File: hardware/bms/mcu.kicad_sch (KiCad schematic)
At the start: 0 parts

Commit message: More charger sch progress
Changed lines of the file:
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@@
     (effects (font (size 1.27 1.27)) (justify right))
+  )
+  (hierarchical_label "PWM_OUT1" (shape output) (at 130.81 40.64 0) (fields_autoplaced)
+    (effects (font (size 1.27 1.27)) (justify left))
   )
   (hierarchical_label "MCU_VIN" (shape input) (at 49.53 40.64 180) (fields_autoplaced)
@@
     (effects (font (size 1.27 1.27)) (justify right))
   )
+  (hierarchical_label "PWM_OUT2" (shape output) (at 130.81 44.45 0) (fields_autoplaced)
+    (effects (font (size 1.27 1.27)) (justify left))
+  )
 )

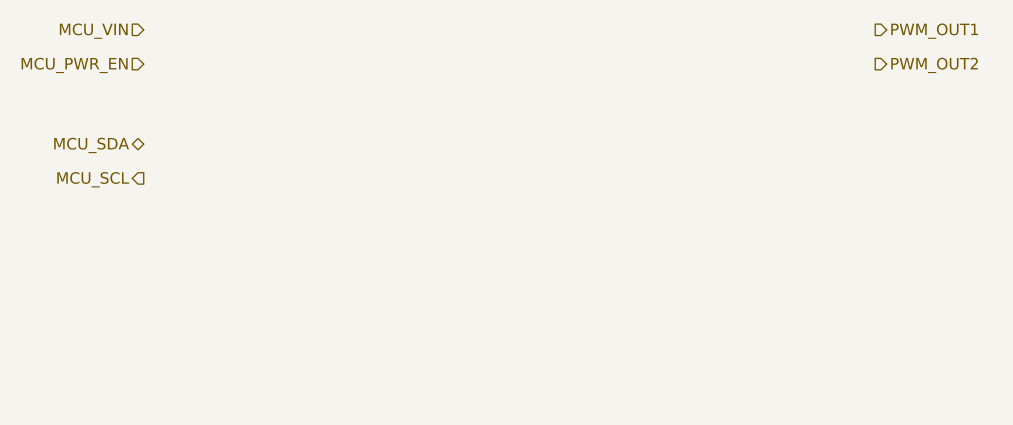
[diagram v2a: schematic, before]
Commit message: Made more progress on charger sch. Need to complete power stage next. Also added diode OR for MCU power conv input. Still deciding on converter selection
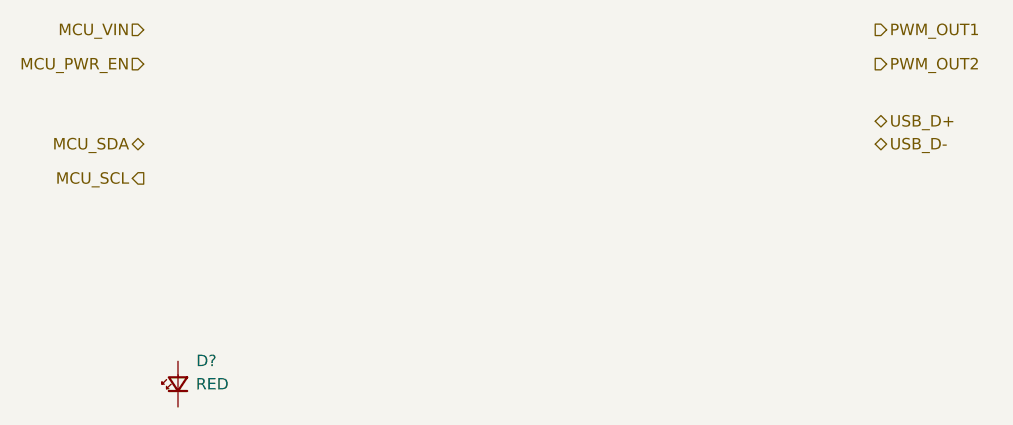
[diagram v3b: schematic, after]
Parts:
- added D?: RED, LED_SMD:LED_0603_1608Metric, symbol Device:LED_Small
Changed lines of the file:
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@@
     (effects (font (size 1.27 1.27)) (justify right))
+  )
+  (hierarchical_label "USB_D+" (shape bidirectional) (at 130.81 50.8 0) (fields_autoplaced)
+    (effects (font (size 1.27 1.27)) (justify left))
   )
   (hierarchical_label "PWM_OUT1" (shape output) (at 130.81 40.64 0) (fields_autoplaced)
@@
     (effects (font (size 1.27 1.27)) (justify right))
   )
+  (hierarchical_label "USB_D-" (shape bidirectional) (at 130.81 53.34 0) (fields_autoplaced)
+    (effects (font (size 1.27 1.27)) (justify left))
+  )
   (hierarchical_label "MCU_SDA" (shape bidirectional) (at 49.53 53.34 180) (fields_autoplaced)
     (effects (font (size 1.27 1.27)) (justify right))
@@
     (effects (font (size 1.27 1.27)) (justify left))
   )
+  (symbol (lib_id "Device:LED_Small") (at 53.34 80.01 90) (unit 1)
+    (in_bom yes) (on_board yes) (dnp no)
+    (property "Reference" "D?" (at 56.5003 77.4194 90)
+      (effects (font (size 1.27 1.27)))
+    )
+    (property "Value" "RED" (at 57.15 80.01 90)
+      (effects (font (size 1.27 1.27)))
+    )
+    (property "Footprint" "LED_SMD:LED_0603_1608Metric" (at 53.34 80.01 90)
+      (effects (font (size 1.27 1.27)) hide)
+    )
+    (property "Datasheet" "~" (at 53.34 80.01 90)
+      (effects (font (size 1.27 1.27)) hide)
+    )
+    (property "MFG" "Würth Elektronik" (at 53.34 80.01 90)
+      (effects (font (size 1.27 1.27)) hide)
+    )
+    (property "MFG PN" "150060RS75000" (at 53.34 80.01 90)
+      (effects (font (size 1.27 1.27)) hide)
+    )
+    (property "VF" "2V" (at 53.34 80.01 90)
+      (effects (font (size 1.27 1.27)) hide)
+    )
+    (pin "1")
+    (pin "2")
+    (instances
+      (project "bms"
+        (path "/a4805e9d-b940-444e-a7cb-db4f4c53ed46/00000000-0000-0000-0000-00006523ab32"
+          (reference "D?") (unit 1)
+        )
+        (path "/a4805e9d-b940-444e-a7cb-db4f4c53ed46/00000000-0000-0000-0000-00006658c265"
+          (reference "D?") (unit 1)
+        )
+      )
+    )
+  )
 )

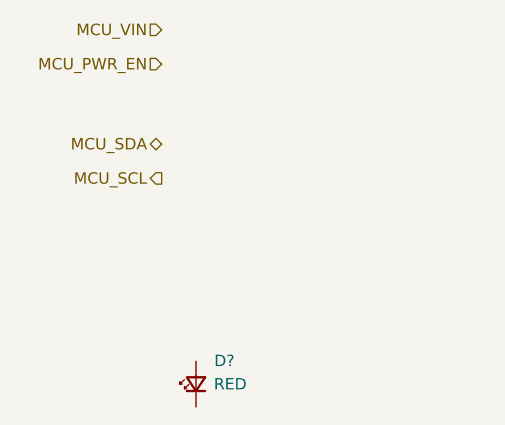
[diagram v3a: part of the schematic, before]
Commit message: Charger schematic complete! Only MCU left.
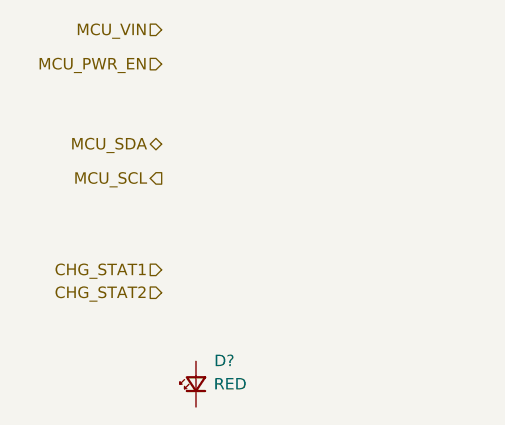
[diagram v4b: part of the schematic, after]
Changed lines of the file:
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@@
     (effects (font (size 1.27 1.27)) (justify left))
+  )
+  (hierarchical_label "CHG_STAT2" (shape input) (at 49.53 69.85 180) (fields_autoplaced)
+    (effects (font (size 1.27 1.27)) (justify right))
   )
   (hierarchical_label "PWM_OUT1" (shape output) (at 130.81 40.64 0) (fields_autoplaced)
@@
     (effects (font (size 1.27 1.27)) (justify left))
   )
+  (hierarchical_label "CHG_STAT1" (shape input) (at 49.53 67.31 180) (fields_autoplaced)
+    (effects (font (size 1.27 1.27)) (justify right))
+  )
   (symbol (lib_id "Device:LED_Small") (at 53.34 80.01 90) (unit 1)

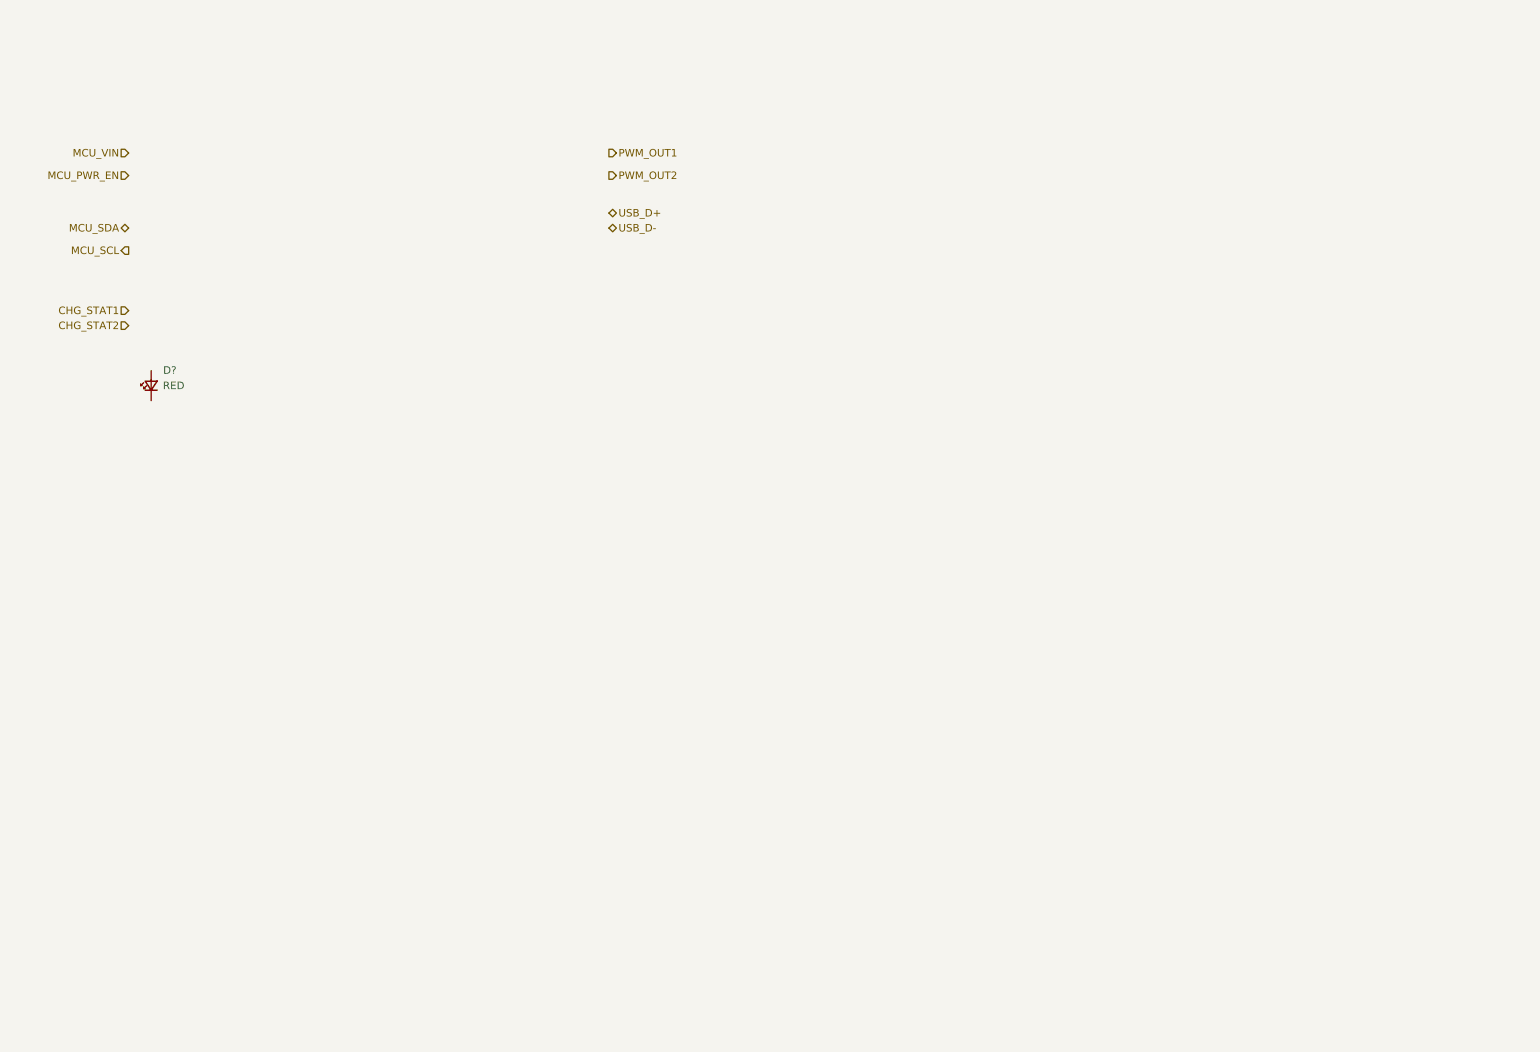
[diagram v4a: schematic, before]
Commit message: Choose MCU as ESP32-C3-MINI. Small form factor with just enough I/O.
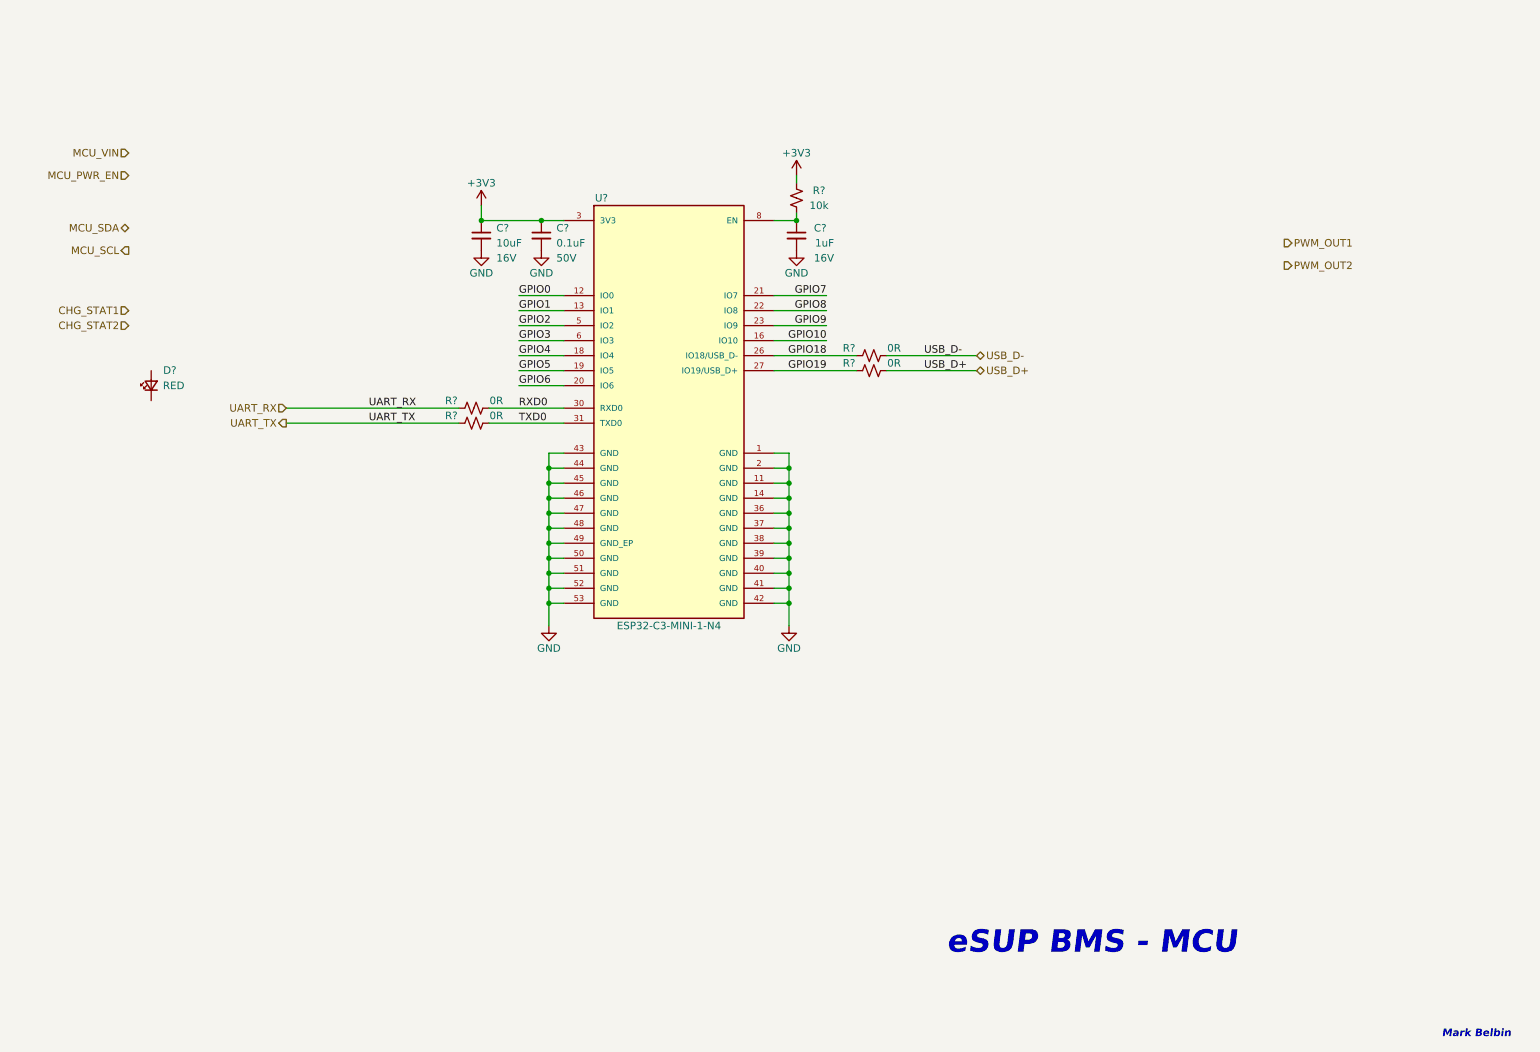
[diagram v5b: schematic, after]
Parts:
- added C?: 0.1uF, Capacitor_SMD:C_0603_1608Metric, symbol Device:C_Small
- added C?: 1uF, Capacitor_SMD:C_0603_1608Metric, symbol Device:C_Small
- added C?: 10uF, Capacitor_SMD:C_0603_1608Metric, symbol Device:C_Small
- added R? (x4): 0R, Resistor_SMD:R_0603_1608Metric, symbol Device:R_Small_US
- added R?: 10k, Resistor_SMD:R_0603_1608Metric, symbol Device:R_Small_US
- added U?: ESP32-C3-MINI-1-N4, bms:ESP32-C3-MINI-1, symbol bms:ESP32-C3-MINI-1-N4
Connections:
- net USB_D+: now also R?.2
- net USB_D-: now also R?.2
- new net: C?.1, R?.2, U?.8 (EN)
- new net: U?.10 (NC), U?.15 (NC), U?.17 (NC), U?.24 (NC), U?.25 (NC), U?.28 (NC), U?.29 (NC), U?.32 (NC), U?.33 (NC), U?.34 (NC), U?.35 (NC), U?.4 (NC), U?.7 (NC), U?.9 (NC)
- new net +3V3: C?.1, C?.1, R?.1, U?.3 (3V3)
- new net GND: C?.2, C?.2, C?.2, U?.1 (GND), U?.11 (GND), U?.14 (GND), U?.2 (GND), U?.36 (GND), U?.37 (GND), U?.38 (GND), U?.39 (GND), U?.40 (GND), U?.41 (GND), U?.42 (GND), U?.43 (GND), U?.44 (GND), U?.45 (GND), U?.46 (GND), U?.47 (GND), U?.48 (GND), U?.49 (GND_EP), U?.50 (GND), U?.51 (GND), U?.52 (GND), U?.53 (GND)
- new net GPIO0: U?.12 (IO0)
- new net GPIO1: U?.13 (IO1)
- new net GPIO10: U?.16 (IO10)
- new net GPIO18: R?.1, U?.26 (IO18/USB_D-)
- new net GPIO19: R?.1, U?.27 (IO19/USB_D+)
- new net GPIO2: U?.5 (IO2)
- new net GPIO3: U?.6 (IO3)
- new net GPIO4: U?.18 (IO4)
- new net GPIO5: U?.19 (IO5)
- new net GPIO6: U?.20 (IO6)
- new net GPIO7: U?.21 (IO7)
- new net GPIO8: U?.22 (IO8)
- new net GPIO9: U?.23 (IO9)
- new net RXD0: R?.2, U?.30 (RXD0)
- new net TXD0: R?.2, U?.31 (TXD0)
- new net UART_RX: R?.1
- new net UART_TX: R?.1
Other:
- note added: "Mark Belbin"
- note added: "eSUP BMS - MCU"

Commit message: Added BJT to enable BMS/MCU when charger input voltage present
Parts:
- added C?: 0.1uF, Capacitor_SMD:C_0603_1608Metric, symbol Device:C_Small
- added D?: WS2812B, LED_SMD:LED_WS2812B_PLCC4_5.0x5.0mm_P3.2mm, symbol LED:WS2812B
- added U?: SN74LXC1T14DCKR, bms:DCK0005A-IPC_C, symbol bms:SN74LXC1T14DCKR
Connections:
- net +3V3: now also U?.1 (VCCI)
- net GND: now also C?.2, D?.3 (VSS), U?.3 (GND)
- new net +5V: C?.1, D?.1 (VDD), U?.5 (VCCO)
- new net RGB_DIN: D?.4 (DIN), U?.4 (Y)
- new net RGB_DIN_ESP: U?.2 (A)
- new net RGB_DOUT: D?.2 (DOUT)
- no-connect marks 0 -> 1
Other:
- moved on the sheet: C?, R?, U?

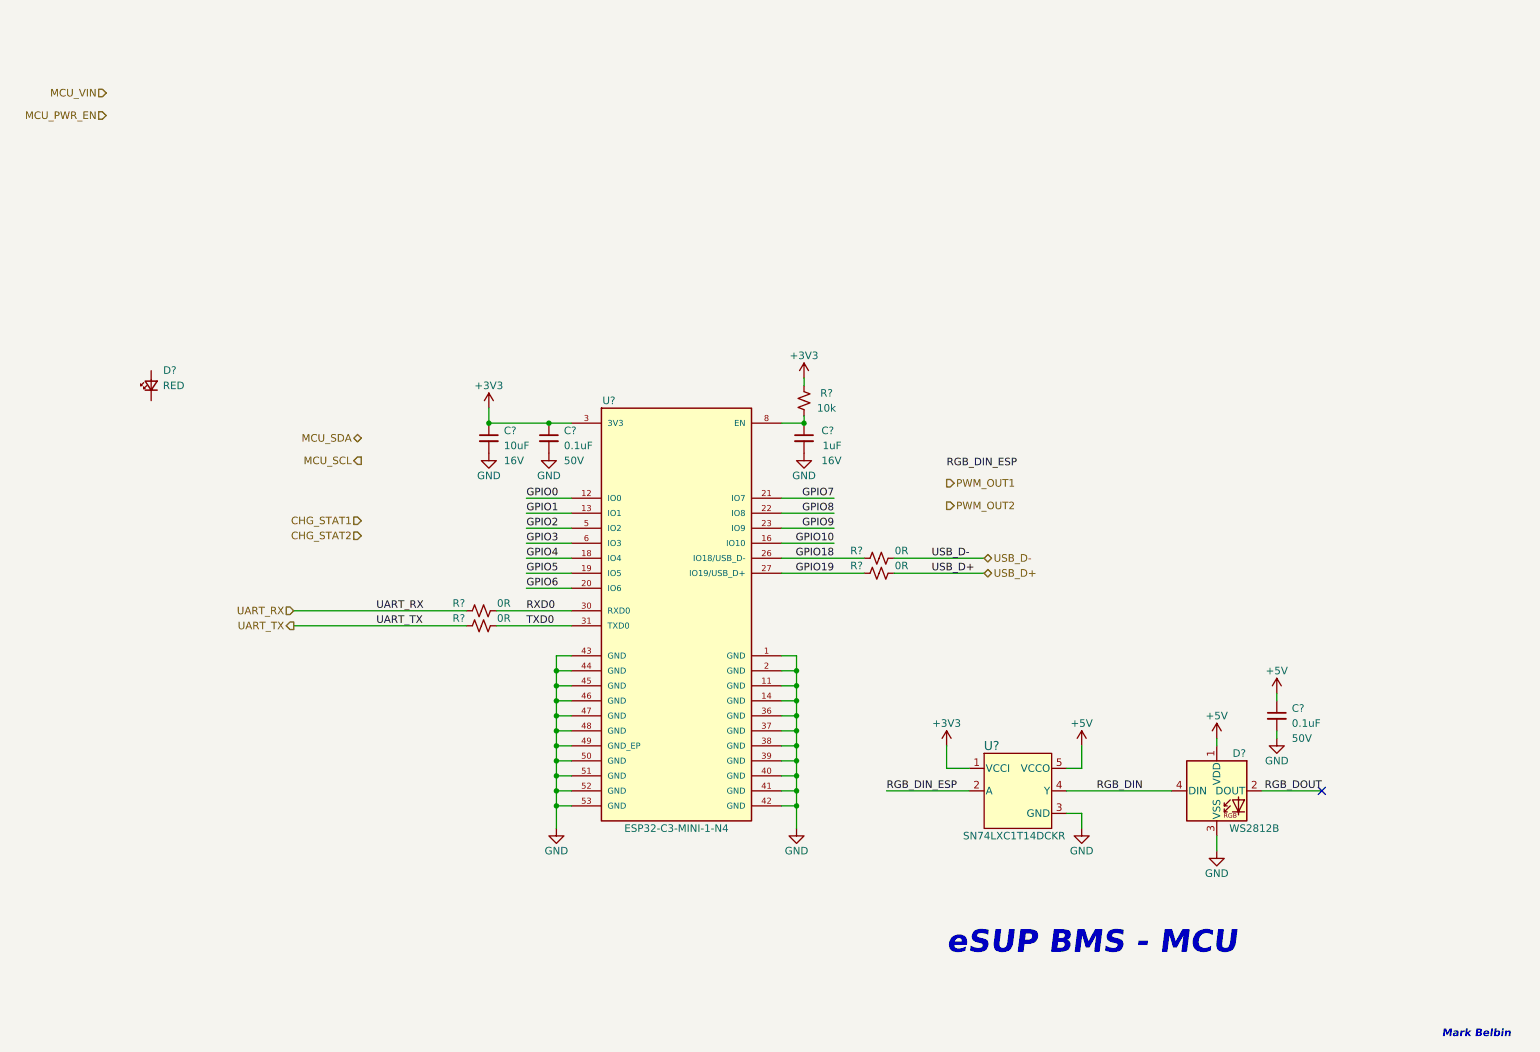
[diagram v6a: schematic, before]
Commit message: Selected power conversion scheme and converters.
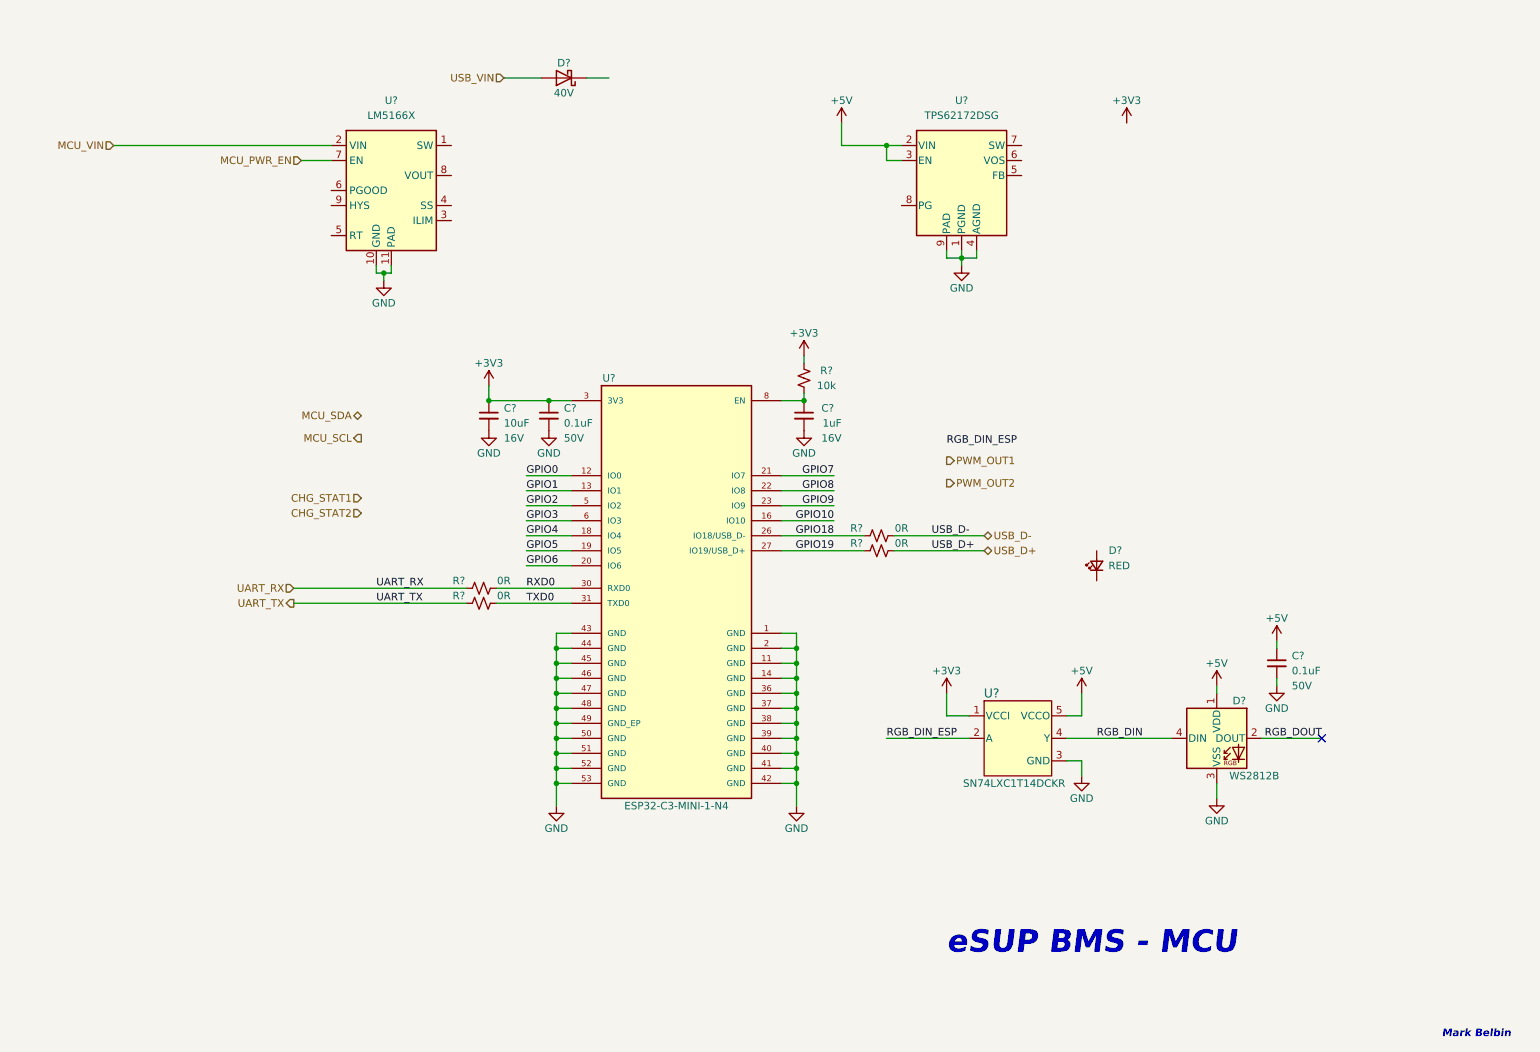
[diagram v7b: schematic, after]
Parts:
- added D?: D_Schottky, Diode_SMD:D_SOD-123, symbol Device:D_Schottky
- added U?: LM5166X, Package_SON:Texas_S-PVSON-N10_ThermalVias, symbol Regulator_Switching:LM5166X
- added U?: TPS62172DSG, Package_SON:WSON-8-1EP_2x2mm_P0.5mm_EP0.9x1.6mm_ThermalVias, symbol Regulator_Switching:TPS62172DSG
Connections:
- net +5V: now also U?.2 (VIN), U?.3 (EN)
- net GND: now also U?.1 (PGND), U?.10 (GND), U?.11 (PAD), U?.4 (AGND), U?.9 (PAD)
- net MCU_PWR_EN: now also U?.7 (EN)
- net MCU_VIN: now also U?.2 (VIN)
- new net USB_VIN: D?.2 (A)
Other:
- moved on the sheet: C?, D?, R?, U?
